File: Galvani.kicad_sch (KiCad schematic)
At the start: 72 parts, among them J1 USB-C Receptacle, J2 U.FL Connector, P1 Cap 1.5pF 0402, P2 L 2.7 nH 0201, P3 Cap 1.5pF 0402, SW1 Pushbutton 4.2x3.2mm 250gf, SW2 Pushbutton 4.2x3.2mm 250gf, U1 TPS560430, U2 ESP32-C3FN4, U3 W25Q128JVS, U4 SN74LVC4245APWR, U5 TPS560430, Y1 Crystal 40MHz 2016

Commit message: layout complete
Signed-off-by: Sean Cross <sean@xobs.io>
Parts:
- added AE1: PCB Antenna, RF_Antenna:Texas_SWRA117D_2.4GHz_Right, symbol Device:Antenna_Shield
- added CONN4: 2060-453/998-404, Galvani:CONN-SMD_2060-453, symbol Galvani:2060-453/998-404
- added J3, J4: JST-PH, Connector_JST:JST_PH_S3B-PH-SM4-TB_1x03-1MP_P2.00mm_Horizontal, symbol Connector_Generic:Conn_01x03
- added R16, R17: R 20k 0402, Resistor_SMD:R_0402_1005Metric, symbol Gibraltar:R 20k 0402
- C6, C7: value Cap 12pF 0402 -> Cap 12pF 0201; footprint Capacitor_SMD:C_0402_1005Metric -> Capacitor_SMD:C_0201_0603Metric
- CONN2: value 2060-453/998-404 -> Bare Wire
- L2, P2: footprint Inductor_SMD:L_0402_1005Metric -> Inductor_SMD:L_0201_0603Metric
- P1, P3: value Cap 1.5pF 0402 -> Cap 1.5pF 0201; footprint Capacitor_SMD:C_0402_1005Metric -> Capacitor_SMD:C_0201_0603Metric
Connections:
- net Earth: now also CONN4.3
- net GND: now also J1.A1B12 (GND), J1.B1A12 (GND), AE1.2 (Shield), J3.3 (Pin_3), J4.3 (Pin_3); no longer J1.A1 (GND), J1.A12 (GND), J1.B1 (GND), J1.B12 (GND)
- net LED_EXTERNAL_5V: now also J3.2 (Pin_2)
- net V5V: now also J3.1 (Pin_1), J4.1 (Pin_1)
- net VAC: now also CONN4.1
- net VUSB: now also J1.A4B9 (VBUS), J1.B4A9 (VBUS); no longer J1.A4 (VBUS), J1.A9 (VBUS), J1.B4 (VBUS), J1.B9 (VBUS)
- net VWIFI: no longer C8.1, R7.2, SW2.2, U2.7 (CHIP_EN)
- net at P1.2, P2.1: now also R16.1, R17.2; no longer J2.1 (In)
- net at CONN2.2, D9.1 (DOUT): now also J4.2 (Pin_2)
- new net: J2.1 (In), R17.1
- new net: AE1.1 (A), R16.2
- new net RESET: C8.1, R7.2, SW2.2, U2.7 (CHIP_EN)
- no-connect marks 20 -> 21
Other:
- note added: "External LEDs"
- moved on the sheet: C8, CONN1, CONN2, CONN3, J1, J2

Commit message: evt1: initial release
Signed-off-by: Sean Cross <sean@xobs.io>
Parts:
- removed C17: 22uF, Capacitor_SMD:C_0805_2012Metric, symbol Device:C
- removed C19, C3: Cap 12pF 0402, Capacitor_SMD:C_0402_1005Metric, symbol Gibraltar:Cap 12pF 0402
- removed L2: L 20nH 0201, Inductor_SMD:L_0201_0603Metric, symbol Gibraltar:L 20nH 0402
- removed R12, R13, R14: R 20k 0402, Resistor_SMD:R_0402_1005Metric, symbol Gibraltar:R 20k 0402
- removed U1: TPS560430, Package_TO_SOT_SMD:SOT-23-6, symbol Bne800:TPS560430
- removed U4: SN74LVC4245APWR, Galvani:TSSOP-24_L7.8-W4.4-P0.65-LS6.4-BL, symbol Galvani:SN74LVC4245APWR
- added C17, C20, C21, C3, C5: Cap 100nF 0402, Capacitor_SMD:C_0402_1005Metric, symbol Gibraltar:Cap 1uF 0402
- added C19: 1.8mF, Galvani:CAP-SMD_BD18.0-L21.5-W21.5, symbol Device:C_Polarized
- added C30, C31: Cap 10uF 0805, Capacitor_SMD:C_0805_2012Metric, symbol Gibraltar:Cap 100nF 0402
- added C32: Cap 10nF 0402, Capacitor_SMD:C_0402_1005Metric, symbol Gibraltar:Cap 10nF 0402
- added D12: SS34, Diode_SMD:D_SMA, symbol Diode:SS34
- added H2, H3: Mounting Hole, MountingHole:MountingHole_3.5mm, symbol Mechanical:MountingHole
- added L4: L 2.7 nH 0201, Inductor_SMD:L_0201_0603Metric, symbol Gibraltar:L 2.7 nH 0402
- added R18: R 20k 0402, Resistor_SMD:R_0402_1005Metric, symbol Gibraltar:R 20k 0402
- added TP1: GND, Galvani:Test Point, symbol Connector:TestPoint
- added TP2: 5V, Galvani:Test Point, symbol Connector:TestPoint
- added U1: LMR14030SDDAR, Package_SO:SOIC-8-1EP_3.9x4.9mm_P1.27mm_EP2.41x3.3mm_ThermalVias, symbol Galvani:LMR14030SDDAR
- added U4, U6: SN74LVC1T45DBVR, Package_TO_SOT_SMD:SOT-23-6, symbol Logic_LevelTranslator:SN74LVC1T45DBV
- C1, C2: value 10mF -> 1.8mF; footprint Galvani:CAP-SMD_BD16.0-L17.0-W17.0-FD -> Galvani:CAP-SMD_BD18.0-L21.5-W21.5; LCSC C239251 -> C3029717; MPN VT1H102M1616 -> VUX182M1VTR-1821; Manufacturer ROQANG -> Lelon
- C14: value Cap 100nF 0402 -> Cap 22uF 0805; footprint Capacitor_SMD:C_0402_1005Metric -> Capacitor_SMD:C_0805_2012Metric; LCSC (none) -> C45783; MPN CL05A104KA5NNNC -> CL21A226MAQNNNE; Manufacturer Samsung Electro-Mechanics -> Samsung electro-mechanics; Val 100nF -> 22uF
- C18, C4: value Cap 22uF 0808 -> Cap 22uF 0805
- CONN1: value 2060-453/998-404 -> Bare Wire
- CONN3, CONN4: value 2060-453/998-404 -> Wire Connector; footprint Galvani:CONN-SMD_2060-453 -> Galvani:CONN-SMD_2060-452; symbol Galvani:2060-453/998-404 -> Galvani:2060-452/998-404; LCSC C2765056 -> C2765055; MPN 2060-453/998-404 -> 2060-452/998-404
- D1: value DB207S -> DB307S; LCSC C3011147 -> C3011148; MPN DB207S -> DB307S
- F1: LCSC (none) -> C2838983; MPN (none) -> SRF1206P150; Manufacturer (none) -> Prosemi
- L1: value 22uH -> 4.7uH; footprint Galvani:IND-SMD_L7.1-W6.6 -> Galvani:IND-SMD_L7.2-W6.6_GPSR07X0; LCSC C497873 -> C5189748; MPN YSPI0630A-220M -> CYA0630-4.7UH; Manufacturer YJYCOIN -> SHOU HAN
- P1: LCSC (none) -> C161414; MPN (none) -> GRM0335C1H1R5BA01D; Manufacturer (none) -> Murata
- P3: MPN (none) -> GRM0335C1H1R5BA01D; Manufacturer (none) -> Murata
- R10: Val 0 Ohm -> 20k
- R15: Val 100k -> 51k
- R2: Val 100k -> 68k
- R3: Val 22.1k -> 12k
- U3: LCSC (none) -> C97521; MPN (none) -> W25Q128JVSIQ; Manufacturer (none) -> Winbond Elec
- Y1: LCSC (none) -> C648971; MPN XRCGB40M000F1S1BR0 -> 7D040000F01; Manufacturer Murata Electronics -> HD
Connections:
- net Earth: now also CONN4.2; no longer CONN4.3
- net GND: now also C14.2, CONN1.3, CONN2.3, J3.MP, J4.MP, R10.1, U2.4 (XTAL_32K_P/ADC1_CH0), U2.5 (XTAL_32K_N/ADC1_CH1), C19.2, C20.1, C21.2, C30.2, C31.2, C32.1, C5.2, D12.2 (A), R18.1, TP1.1, U1.7 (GND), U1.9 (EPAD), U4.2 (GND), U6.2 (GND); no longer C14.1, CONN1.1, CONN2.1, R10.2
- net LED_EXTERNAL: now also U6.3 (A)
- net LED_EXTERNAL_5V: now also U6.4 (B)
- net LED_INTERNAL: now also U4.3 (A)
- net LED_INTERNAL_5V: now also U4.4 (B)
- net V5V: now also C14.1, CONN1.1, CONN2.1, C21.1, TP2.1, U4.6 (VCCB), U6.6 (VCCB); no longer CONN1.3, CONN2.3
- net VAC: now also CONN3.2; no longer CONN3.3
- net VAC_RECTIFIED: now also C19.1, C30.1, C31.1, U1.2 (VIN), U1.3 (EN)
- net VSPI: now also C5.1; no longer C14.2
- net VWIFI: now also C20.2, L4.2, U4.1 (VCCA), U4.5 (DIR), U6.1 (VCCA), U6.5 (DIR); no longer C10.1, U2.2 (VDD3P3), U2.3 (VDD3P3)
- net at R2.1, R3.1: now also U1.5 (FB)
- net at L1.1: now also C17.1, D12.1 (K), U1.8 (SW)
- net at U5.1 (CB): now also C3.2
- net at L3.1, U5.6 (SW): now also C3.1
- net at U2.30 (XTAL_P): now also C6.1, Y1.1
- new net: J1.1 (Shell), J1.2 (Shell), J1.3 (Shell), J1.4 (Shell), R18.2
- new net: R10.2, U1.4 (RT/SYNC)
- new net: C17.2, U1.1 (BOOT)
- new net: C32.2, U1.6 (SS)
- new net: C10.1, L4.1, U2.2 (VDD3P3), U2.3 (VDD3P3)
- no-connect marks 21 -> 9
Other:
- note added: "GND indicates EVT1"
- note added: "Level Shifters"
- note added: "Test Points and Mounting Holes"
- moved on the sheet: C10, C11, C12, C13, C15, C16, C2, C22, C23, C24, C25, C26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

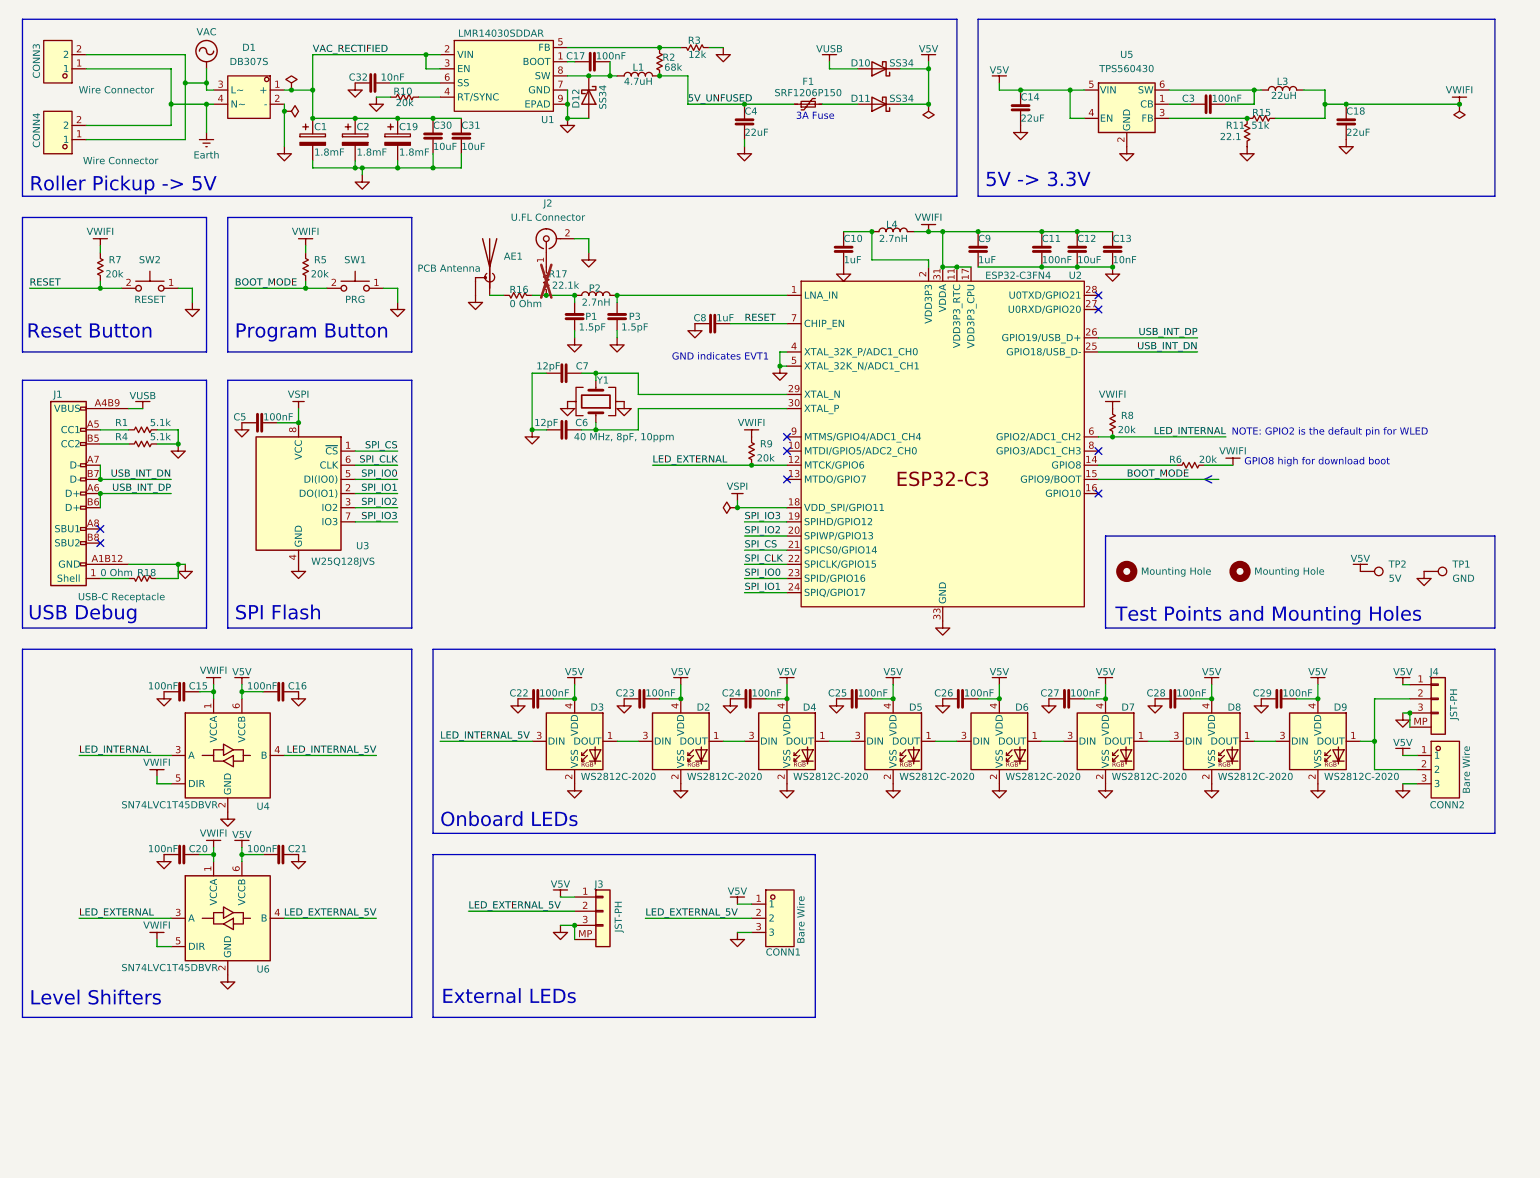
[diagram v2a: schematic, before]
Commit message: evt2: finish pcb
Signed-off-by: Sean Cross <sean@xobs.io>
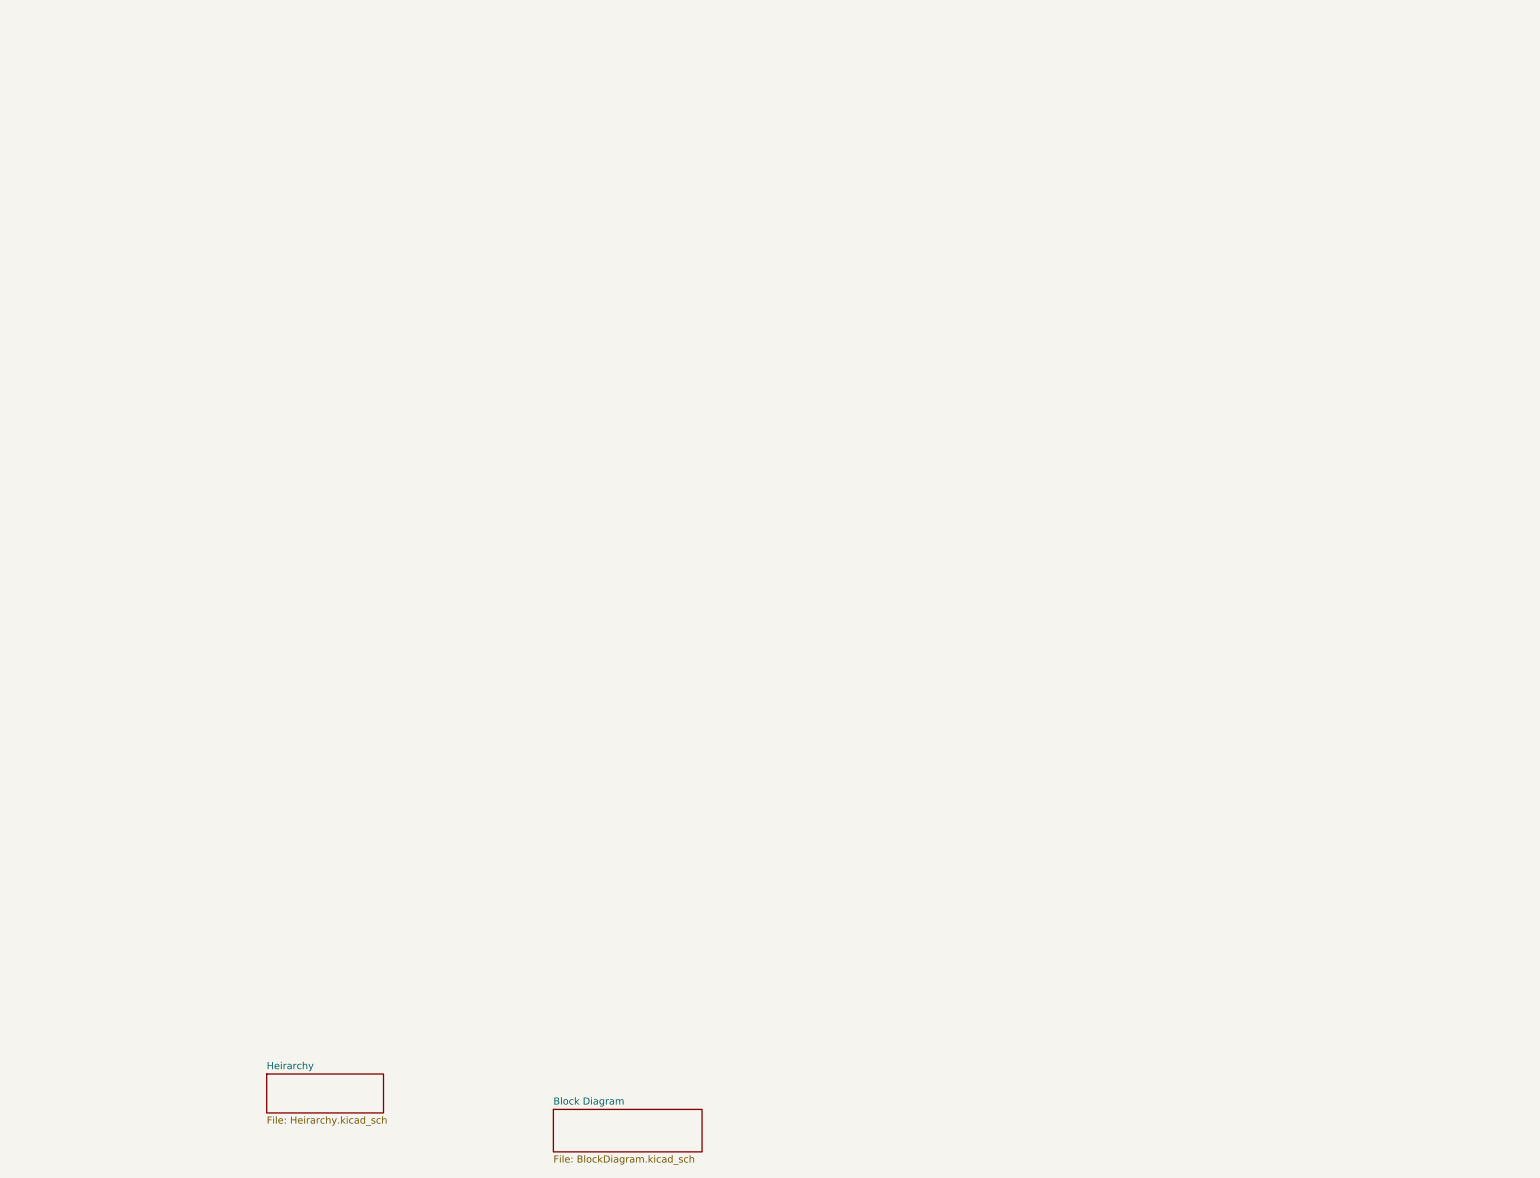
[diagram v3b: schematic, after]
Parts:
- removed AE1: PCB Antenna, RF_Antenna:Texas_SWRA117D_2.4GHz_Right, symbol Device:Antenna_Shield
- removed C1, C19, C2: 1.8mF, Galvani:CAP-SMD_BD18.0-L21.5-W21.5, symbol Device:C_Polarized
- removed C10, C9: Cap 1uF 0402, Capacitor_SMD:C_0402_1005Metric, symbol Gibraltar:Cap 100nF 0402
- removed C11: Cap 100nF 0402, Capacitor_SMD:C_0402_1005Metric, symbol Gibraltar:Cap 100nF 0402
- removed C12: Cap 10uF 0603, Capacitor_SMD:C_0603_1608Metric, symbol Gibraltar:Cap 10uF 0603
- removed C13, C32: Cap 10nF 0402, Capacitor_SMD:C_0402_1005Metric, symbol Gibraltar:Cap 10nF 0402
- removed C14, C18, C4: Cap 22uF 0805, Capacitor_SMD:C_0805_2012Metric, symbol Gibraltar:Cap 100nF 0402
- removed C15, C16, C17, C20, C21, C22, C23, C24, C25, C26, C27, C28, C29, C3, C5: Cap 100nF 0402, Capacitor_SMD:C_0402_1005Metric, symbol Gibraltar:Cap 1uF 0402
- removed C30, C31: Cap 10uF 0805, Capacitor_SMD:C_0805_2012Metric, symbol Gibraltar:Cap 100nF 0402
- removed C6, C7: Cap 12pF 0201, Capacitor_SMD:C_0201_0603Metric, symbol Gibraltar:Cap 12pF 0402
- removed C8: Cap 1uF 0402, Capacitor_SMD:C_0402_1005Metric, symbol Gibraltar:Cap 1uF 0402
- removed CONN1, CONN2: Bare Wire, Galvani:CONN-SMD_2060-453, symbol Galvani:2060-453/998-404
- removed CONN3, CONN4: Wire Connector, Galvani:CONN-SMD_2060-452, symbol Galvani:2060-452/998-404
- removed D1: DB307S, Galvani:DB-S_L8.3-W6.4-P5.10-LS9.9-TL, symbol Galvani:DB207S
- removed D10, D11, D12: SS34, Diode_SMD:D_SMA, symbol Diode:SS34
- removed D2, D3, D4, D5, D6, D7, D8, D9: WS2812C-2020, Galvani:LED_WS2812B-2020_PLCC4_2.0x2.0mm, symbol Galvani:WS2812C-2020
- removed F1: SRF1206P150, Fuse:Fuse_1206_3216Metric, symbol Device:Polyfuse_Small
- removed H2, H3: Mounting Hole, MountingHole:MountingHole_3.5mm, symbol Mechanical:MountingHole
- removed J1: USB-C Receptacle, Galvani:USB-C-SMD_TYPE-C16PIN, symbol Gibraltar:USB-C_Receptacle_PCB
- removed J2: U.FL Connector, Connector_Coaxial:U.FL_Hirose_U.FL-R-SMT-1_Vertical, symbol Connector:Conn_Coaxial
- removed J3, J4: JST-PH, Connector_JST:JST_PH_S3B-PH-SM4-TB_1x03-1MP_P2.00mm_Horizontal, symbol Connector_Generic:Conn_01x03
- removed L1: 4.7uH, Galvani:IND-SMD_L7.2-W6.6_GPSR07X0, symbol Galvani:YSPI0630A-220M
- removed L3: 22uH, Galvani:IND-SMD_L7.1-W6.6, symbol Galvani:YSPI0630A-220M
- removed L4, P2: L 2.7 nH 0201, Inductor_SMD:L_0201_0603Metric, symbol Gibraltar:L 2.7 nH 0402
- removed P1: Cap 1.5pF 0201, Capacitor_SMD:C_0201_0603Metric, symbol Gibraltar:Cap 2.4pF 0402
- removed P3: Cap 1.5pF 0201, Capacitor_SMD:C_0201_0603Metric, symbol Gibraltar:Cap 3.9pF 0402
- removed R1, R4: R 5.1k 0402, Resistor_SMD:R_0402_1005Metric, symbol Gibraltar:R 5.1k 0402
- removed R10, R15, R16, R17, R18, R2, R3, R5, R6, R7, R8, R9: R 20k 0402, Resistor_SMD:R_0402_1005Metric, symbol Gibraltar:R 20k 0402
- removed R11: R 22.1k 0402, Resistor_SMD:R_0402_1005Metric, symbol Gibraltar:R 20k 0402
- removed SW1, SW2: Pushbutton 4.2x3.2mm 250gf, Button_Switch_SMD:SW_Push_1P1T_XKB_TS-1187A, symbol Galvani:Pushbutton_Basic
- removed TP1: GND, Galvani:Test Point, symbol Connector:TestPoint
- removed TP2: 5V, Galvani:Test Point, symbol Connector:TestPoint
- removed U1: LMR14030SDDAR, Package_SO:SOIC-8-1EP_3.9x4.9mm_P1.27mm_EP2.41x3.3mm_ThermalVias, symbol Galvani:LMR14030SDDAR
- removed U2: ESP32-C3FN4, Package_DFN_QFN:QFN-32-1EP_5x5mm_P0.5mm_EP3.45x3.45mm, symbol Espressif:ESP32-C3
- removed U3: W25Q128JVS, Package_SO:SOIC-8_5.23x5.23mm_P1.27mm, symbol Memory_Flash:W25Q128JVS
- removed U4, U6: SN74LVC1T45DBVR, Package_TO_SOT_SMD:SOT-23-6, symbol Logic_LevelTranslator:SN74LVC1T45DBV
- removed U5: TPS560430, Package_TO_SOT_SMD:SOT-23-6, symbol Bne800:TPS560430
- removed Y1: Crystal 40MHz 2016, Galvani:Crystal_SMD_2016-4Pin_2.0x1.6mm, symbol Gibraltar:Crystal 40MHz 2016
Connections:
- no-connect marks 9 -> 0
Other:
- added sheet Block Diagram (BlockDiagram.kicad_sch)
- added sheet Heirarchy (Heirarchy.kicad_sch)
- note removed: "3A Fuse"
- note removed: "5V -> 3.3V"
- note removed: "External LEDs"
- note removed: "GND indicates EVT1"
- note removed: "GPIO8 high for download boot"
- note removed: "Level Shifters"
- note removed: "NOTE: GPIO2 is the default pin for WLED"
- note removed: "Onboard LEDs"
- note removed: "Program Button"
- note removed: "Reset Button"
- note removed: "Roller Pickup -> 5V"
- note removed: "SPI Flash"
- note removed: "Test Points and Mounting Holes"
- note removed: "USB Debug"

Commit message: release evt2
Signed-off-by: Sean Cross <sean@xobs.io>
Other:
- note added: "2: Block Diagram"
- note added: "3: Heirarchy"
- note added: "4: Power"
- note added: "5: Audio"
- note added: "6: CPU"
- note added: "7: LEDs"
- note added: "8: SD Card"
- note added: "Default SSID: WLED Default Password: wled1234 Scan to connect:"
- note added: "Galvani"
- note added: "LED Controller for Model Railroads"

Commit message: change schematic version to EVT2
Signed-off-by: Sean Cross <sean@xobs.io>
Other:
- title: (none) -> Galvani
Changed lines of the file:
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@@
 	(generator_version "8.0")
 	(paper "A4")
+	(title_block
+		(title "Galvani")
+		(date "2024-10-13")
+		(rev "EVT2")
+	)
 	(image
 		(at 238.76 123.19)
